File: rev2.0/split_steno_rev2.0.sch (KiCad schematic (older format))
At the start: 6 parts

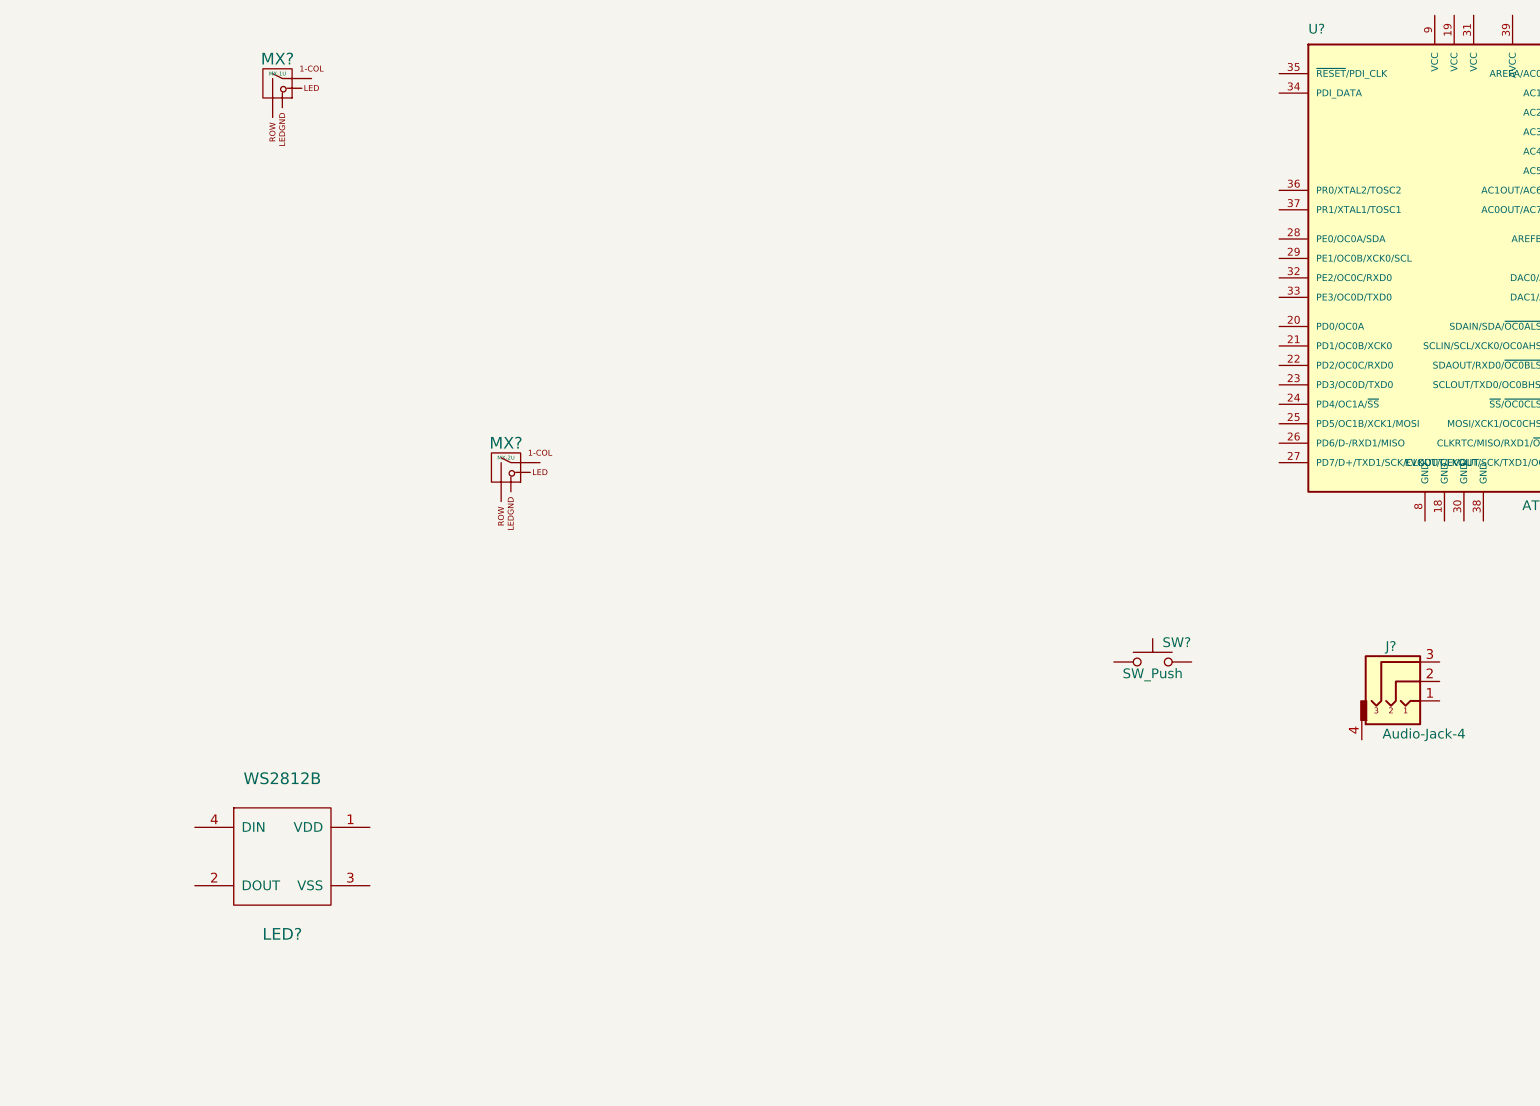
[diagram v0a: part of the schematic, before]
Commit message: switch and underglow matrix
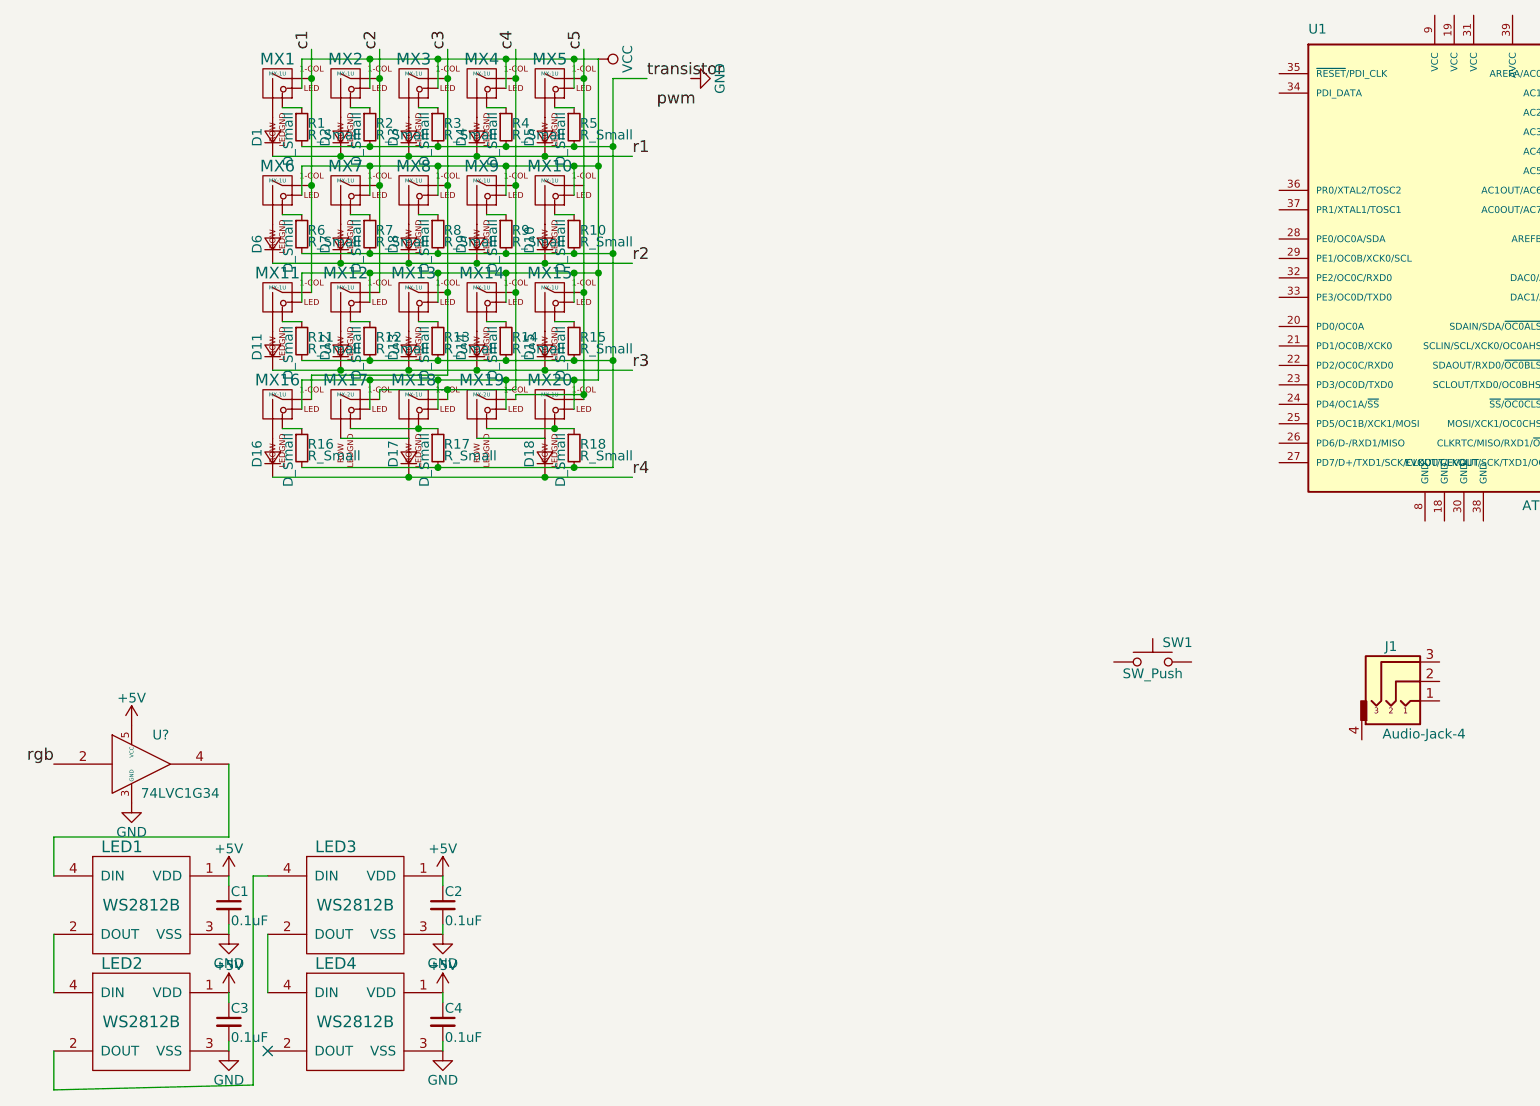
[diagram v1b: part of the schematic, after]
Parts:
- removed LED?: WS2812B, symbol WS2812B
- added C1, C2, C3, C4: 0.1uF, symbol C_Small
- added D1, D10, D11, D12, D13, D14, D15, D16, D17, D18, D2, D3, D4, D5, D6, D7, D8, D9: D_Small, symbol D_Small
- added LED1, LED2, LED3, LED4: WS2812B, symbol WS2812B
- added MX10, MX11, MX12, MX13, MX14, MX15, MX16, MX18, MX2, MX20, MX3, MX4, MX5, MX6, MX7, MX8, MX9: MX-1U, symbol MX-1U
- added MX19: MX-2U, symbol MX-2U
- added R1, R10, R11, R12, R13, R14, R15, R16, R17, R18, R2, R3, R4, R5, R6, R7, R8, R9: R_Small, symbol R_Small
- added U?: 74LVC1G34, symbol 74LVC1G34
- gave numbers to parts that had none: 5
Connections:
- net c1: now reaches MX1.1 (COL)
- net c1: now also MX11.1 (COL), MX6.1 (COL)
- net at MX1.2 (ROW): now also D1.2 (A)
- net VCC: now reaches MX1.3 (LED)
- net VCC: now also MX17.3 (LED), MX10.3 (LED), MX11.3 (LED), MX12.3 (LED), MX13.3 (LED), MX14.3 (LED), MX15.3 (LED), MX16.3 (LED), MX18.3 (LED), MX19.3 (LED), MX2.3 (LED), MX20.3 (LED), MX3.3 (LED), MX4.3 (LED), MX5.3 (LED), MX6.3 (LED), MX7.3 (LED), MX8.3 (LED), MX9.3 (LED)
- net at MX1.4 (LEDGND): now also R1.1
- net c4: now reaches MX17.1 (COL)
- net c4: now also MX14.1 (COL), MX18.1 (COL), MX4.1 (COL), MX9.1 (COL)
- net at MX17.2 (ROW): now also D17.2 (A), MX18.2 (ROW)
- net at MX17.4 (LEDGND): now also MX18.4 (LEDGND), R17.1
- new net: D2.2 (A), MX2.2 (ROW)
- new net: MX2.4 (LEDGND), R2.1
- new net: D3.2 (A), MX3.2 (ROW)
- new net: MX3.4 (LEDGND), R3.1
- new net: D4.2 (A), MX4.2 (ROW)
- new net: MX4.4 (LEDGND), R4.1
- new net: D5.2 (A), MX5.2 (ROW)
- new net: MX5.4 (LEDGND), R5.1
- new net: D18.2 (A), MX19.2 (ROW), MX20.2 (ROW)
- new net: MX19.4 (LEDGND), MX20.4 (LEDGND), R18.1
- new net: D6.2 (A), MX6.2 (ROW)
- new net: MX6.4 (LEDGND), R6.1
- new net: D7.2 (A), MX7.2 (ROW)
- new net: MX7.4 (LEDGND), R7.1
- new net: D8.2 (A), MX8.2 (ROW)
- new net: MX8.4 (LEDGND), R8.1
- new net: D9.2 (A), MX9.2 (ROW)
- new net: MX9.4 (LEDGND), R9.1
- new net: D10.2 (A), MX10.2 (ROW)
- new net: MX10.4 (LEDGND), R10.1
- new net: D11.2 (A), MX11.2 (ROW)
- new net: MX11.4 (LEDGND), R11.1
- new net: D12.2 (A), MX12.2 (ROW)
- new net: MX12.4 (LEDGND), R12.1
- new net: D13.2 (A), MX13.2 (ROW)
- new net: MX13.4 (LEDGND), R13.1
- new net: D14.2 (A), MX14.2 (ROW)
- new net: MX14.4 (LEDGND), R14.1
- new net: D15.2 (A), MX15.2 (ROW)
- new net: MX15.4 (LEDGND), R15.1
- new net: D16.2 (A), MX16.2 (ROW)
- new net: MX16.4 (LEDGND), R16.1
- new net: LED1.2 (DOUT), LED2.4 (DIN)
- new net: LED1.4 (DIN), U?.4
- new net: LED2.2 (DOUT), LED3.4 (DIN)
- new net: LED3.2 (DOUT), LED4.4 (DIN)
- new net +5V: C1.1, C2.1, C3.1, C4.1, LED1.1 (VDD), LED2.1 (VDD), LED3.1 (VDD), LED4.1 (VDD), U?.5 (VCC)
- new net GND: C1.2, C2.2, C3.2, C4.2, LED1.3 (VSS), LED2.3 (VSS), LED3.3 (VSS), LED4.3 (VSS), U?.3 (GND)
- new net c2: MX12.1 (COL), MX2.1 (COL), MX7.1 (COL)
- new net c3: MX13.1 (COL), MX16.1 (COL), MX3.1 (COL), MX8.1 (COL)
- new net c5: MX15.1 (COL), MX19.1 (COL), MX20.1 (COL), MX5.1 (COL)
- new net r1: D1.1 (K), D2.1 (K), D3.1 (K), D4.1 (K), D5.1 (K)
- new net r2: D10.1 (K), D6.1 (K), D7.1 (K), D8.1 (K), D9.1 (K)
- new net r3: D11.1 (K), D12.1 (K), D13.1 (K), D14.1 (K), D15.1 (K)
- new net r4: D16.1 (K), D17.1 (K), D18.1 (K)
- new net rgb: U?.2
- new net transistor: R1.2, R10.2, R11.2, R12.2, R13.2, R14.2, R15.2, R16.2, R17.2, R18.2, R2.2, R3.2, R4.2, R5.2, R6.2, R7.2, R8.2, R9.2
- no-connect marks 0 -> 1
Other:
- moved on the sheet: MX17

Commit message: some updates
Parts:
- removed C1, C2, C3, C4: 0.1uF, symbol C_Small
- added BT?: Battery, symbol Battery
- added BT?: Battery_Cell, symbol Battery_Cell
- added C? (x2): 4.7uF, symbol C
- added C? (x2): 1uF, symbol C
- added C? (x9): 0.1uF, symbol C
- added C?: 47uF, symbol C
- added D?: D_Schottky_x2_KCom_AAK, symbol D_Schottky_x2_KCom_AAK
- added F?: Fuse, symbol Fuse
- added J?: USB_C_Receptacle, symbol USB_C_Receptacle
- added JP? (x3): Jumper, symbol Jumper
- added P?: TC2030-IDC, symbol TC2030-IDC
- added R? (x2): 10k, symbol R
- added R? (x2): 470k, symbol R
- added R? (x4): R, symbol R
- added SW?: Switch-6P-2S2T, symbol Switch-6P-2S2T
- added U?: nRF24L01_module, symbol nRF24L01_module
- added U?: MCP73831, symbol MCP73831
- added U? (x2): MCP1700, TO_SOT_Packages_SMD:SOT-23, symbol MCP1700
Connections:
- net rgb is gone; now on net UNDER_LED: U?.2
- net +5V: now also C?.1, C?.1, C?.1, C?.1, C?.1, F?.2, R?.1, U?.3 (VI), U?.4 (VDD)
- net GND: now also SW1.1, U1.18 (GND), U1.30 (GND), U1.38 (GND), U1.8 (GND), BT?.2 (-), BT?.2 (-), C?.2, C?.2, C?.2, C?.2, C?.2, C?.2, C?.2, C?.2, C?.2, C?.2, C?.2, C?.2, C?.2, C?.2, J?.A1 (GND), J?.A12 (GND), J?.B1 (GND), J?.B12 (GND), P?.6 (P6), R?.2, R?.2, R?.2, R?.2, U?.1 (GND), U?.1 (GND), U?.2 (VSS), U?.2 (VSS)
- net VCC: now also U1.19 (VCC), U1.31 (VCC), U1.39 (AVCC), U1.9 (VCC), C?.1, C?.1, C?.1, C?.1, C?.1, C?.1, D?.3 (K), JP?.2, P?.2 (P2), R?.1, U?.1 (VDD)
- net UNDER_LED: now reaches U1.10 (SDAIN/SDA/~OC0ALS~/OC0A/PC0)
- net VBUS_CHECK: now reaches U1.11 (SCLIN/SCL/XCK0/OC0AHS/OC0B/PC1)
- net VBUS_CHECK: now also R?.1, R?.2
- net BAT_PROG: now reaches U1.12 (SDAOUT/RXD0/~OC0BLS~/OC0C/PC2)
- net BAT_PROG: now also R?.2
- net BAT_STAT: now reaches U1.13 (SCLOUT/TXD0/OC0BHS/OC0D/PC3)
- net BAT_STAT: now also U?.1 (STAT)
- net CSN: now reaches U1.14 (~SS~/~OC0CLS~/OC1A/PC4)
- net CSN: now also U?.4 (CSN)
- net MOSI: now reaches U1.15 (MOSI/XCK1/OC0CHS/OC1B/PC5)
- net MOSI: now also U?.6 (MOSI)
- net MISO: now reaches U1.16 (CLKRTC/MISO/RXD1/~OC0DLS~/PC6)
- net MISO: now also U?.7 (MISO)
- net SCK: now reaches U1.17 (EVOUT/CLKOUT/SCK/TXD1/OC0DHS/PC7)
- net SCK: now also U?.5 (SCK)
- net PDI: now reaches U1.34 (PDI_DATA)
- net PDI: now also P?.1 (P1)
- net RST: now reaches U1.35 (~RESET~/PDI_CLK)
- net RST: now also SW1.2, P?.5 (P5), R?.2
- net BAT_LVL: now reaches U1.5 (ADC9/PB1)
- net BAT_LVL: now also JP?.2, R?.1, R?.2
- net CE: now reaches U1.6 (DAC0/ADC10/PB2)
- net CE: now also U?.3 (CE)
- net IRQ: now reaches U1.7 (DAC1/ACD11/PB3)
- net IRQ: now also U?.8 (IRQ)
- net c1 renamed C1
- net c2 renamed C2
- net c3 renamed C3
- net c4 renamed C4
- net c5 renamed C5
- net r1 renamed R1
- net r2 renamed R2
- net r3 renamed R3
- net r4 renamed R4
- new net: R?.1, U?.5 (PROG)
- new net: F?.1, J?.A4 (VBUS), J?.A9 (VBUS), J?.B4 (VBUS), J?.B9 (VBUS)
- new net: J?.A5 (CC1), R?.1
- new net: J?.B3 (TX2-), J?.B5 (CC2), R?.1
- new net: C?.1, D?.1 (A), U?.2 (VO)
- new net +BATT: D?.2 (A), JP?.1, JP?.2, SW?.1, SW?.4
- new net BAT_IN: BT?.1 (+), C?.1, JP?.1, JP?.1, SW?.2, SW?.5, U?.2 (VO)
- new net BAT_LI_ION: BT?.1 (+), C?.1, R?.1, U?.3 (VBAT), U?.3 (VI)
- new net USB_L_D+: J?.A6 (D+), J?.B6 (D+)
- new net USB_L_D-: J?.A7 (D-), J?.B7 (D-)
- no-connect marks 1 -> 13
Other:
- moved on the sheet: D1, D10, D11, D12, D13, D14, D15, D16, D17, D18, D2, D3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

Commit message: switch to diodeless matrix, usb otg
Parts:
- removed D1, D10, D11, D12, D13, D14, D15, D16, D17, D18, D2, D3, D4, D5, D6, D7, D8, D9: D_Small, symbol D_Small
- removed J?: USB_C_Receptacle, symbol USB_C_Receptacle
- removed MX1, MX10, MX11, MX12, MX13, MX14, MX15, MX16, MX18, MX2, MX20, MX3, MX4, MX5, MX6, MX7, MX8, MX9: MX-1U, symbol MX-1U
- removed MX17, MX19: MX-2U, symbol MX-2U
- removed R1, R10, R11, R12, R13, R14, R15, R16, R17, R18, R2, R3, R4, R5, R6, R7, R8, R9: R_Small, symbol R_Small
- removed R?: R, symbol R
- added J?: USB_OTG, symbol USB_OTG
- added R? (x2): R, symbol R
- added SW? (x20): SW_Push, symbol SW_Push
- R? (x3): value R -> 100k
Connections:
- net GND: now also J1.4, J?.5 (GND), SW?.2, SW?.2, SW?.2, SW?.2, SW?.2, SW?.2, SW?.2, SW?.2, SW?.2, SW?.2, SW?.2, SW?.2, SW?.2, SW?.2, SW?.2, SW?.2, SW?.2, SW?.2, SW?.2, SW?.2
- net SDA: now reaches U1.28 (PE0/OC0A/SDA)
- net SDA: now also J1.3, R?.2
- net SCL: now reaches U1.29 (PE1/OC0B/XCK0/SCL)
- net SCL: now also J1.2, R?.2
- net +3V3: now reaches J1.1
- net +3V3: now also R?.1, R?.1
- net at F?.1: now also J?.1 (VBUS)
- net at R?.1: now also J?.4 (ID)
- new net KEY1: SW?.1
- new net KEY10: SW?.1
- new net KEY11: SW?.1
- new net KEY12: SW?.1
- new net KEY13: SW?.1
- new net KEY14: SW?.1
- new net KEY15: SW?.1
- new net KEY16: SW?.1
- new net KEY17: SW?.1, SW?.1
- new net KEY18: SW?.1, SW?.1
- new net KEY2: SW?.1
- new net KEY3: SW?.1
- new net KEY4: SW?.1
- new net KEY5: SW?.1
- new net KEY6: SW?.1
- new net KEY7: SW?.1
- new net KEY8: SW?.1
- new net KEY9: SW?.1
- new net USB_D+: J?.3 (D+)
- new net USB_D-: J?.2 (D-)
- no-connect marks 13 -> 6
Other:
- moved on the sheet: BT?, C?, D?, F?, J1, JP?, LED1, LED2, LED3, LED4, P?, R?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

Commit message: things
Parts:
- C14: renamed from C?; value 0.1uF -> 10uF
- R7, R9: renamed from R?; value R -> 4.7k
- gave numbers to parts that had none: 55
- renumbered SW1 to SW22, U1 to U5
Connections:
- net labels added: D+, D-
- net labels removed: USB_D+, USB_D-
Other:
- moved on the sheet: BT1, BT2, C1, C10, C11, C12, C13, C14, C2, C3, C4, C5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

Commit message: did footprint associations
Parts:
- BT1: footprint (none) -> Battery_Holders:Keystone_1058_1x2032-CoinCell
- BT2: footprint (none) -> Connectors_JST:JST_PH_S2B-PH-K_02x2.00mm_Angled
- C1, C10, C11, C12, C13, C14, C2, C3, C4, C5, C6, C7, C8, C9: footprint (none) -> Capacitors_SMD:C_0603_HandSoldering
- J1: footprint (none) -> Keebio-Parts:TRRS-PJ-320A
- LED1, LED2, LED3, LED4: footprint (none) -> WS2812B:WS2812B
- R1, R2, R3, R4, R5, R6, R7, R8, R9: footprint (none) -> Resistors_SMD:R_0603_HandSoldering
- SW1, SW10, SW11, SW12, SW13, SW14, SW15, SW16, SW17, SW18, SW2, SW3, SW4, SW5, SW6, SW7, SW8, SW9: footprint (none) -> Keebio-Parts:Hybrid_PCB_100H_Dual_hole
- SW19, SW20: footprint (none) -> Keebio-Parts:Hybrid_PCB_200H-dual-nosilk
- U5: footprint TQFP44 -> Housings_QFP:TQFP-44_10x10mm_Pitch0.8mm
- U6: footprint (none) -> nordic:NRF24L01-Module-SMD
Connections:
- no-connect marks 6 -> 7

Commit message: begin pcb file
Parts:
- D1: footprint (none) -> TO_SOT_Packages_SMD:SOT-23_Handsoldering
- F1: footprint (none) -> Fuse_Holders_and_Fuses:Fuse_SMD1206_HandSoldering
- J2: footprint (none) -> keyboard_parts:USB_miniB
- JP1, JP2, JP3: footprint (none) -> keyboard_parts:SOLDER_JUMPER_2
- P1: footprint (none) -> Connectors:Tag-Connect_TC2030-IDC-NL
- SW21: footprint (none) -> switch:SlideSwitch_C&K_JS202011CQN
- SW22: footprint (none) -> switch:SwitchPush_C&K_MultiFoot_RS-187R05A2-DS_And_PTS645_SMT
- U1: footprint (none) -> TO_SOT_Packages_SMD:SOT-353_SC-70-5_Handsoldering
- U2: footprint (none) -> TO_SOT_Packages_SMD:SOT-23-5_HandSoldering
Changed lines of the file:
@@
 F 0 "SW22" H 8475 5000 50  0000 L CNN
 F 1 "SW_Push" H 8425 4840 50  0000 C CNN
-F 2 "" H 8425 5100 50  0001 C CNN
+F 2 "switch:SwitchPush_C&K_MultiFoot_RS-187R05A2-DS_And_PTS645_SMT" H 8425 5100 50  0001 C CNN
 F 3 "" H 8425 5100 50  0001 C CNN
 	1    8425 4900
@@
 F 0 "U1" H 2375 5725 50  0000 C CNN
 F 1 "74LVC1G34" H 2475 5425 50  0000 C CNN
-F 2 "" H 2275 5575 50  0001 C CNN
+F 2 "TO_SOT_Packages_SMD:SOT-353_SC-70-5_Handsoldering" H 2275 5575 50  0001 C CNN
 F 3 "" H 2275 5575 50  0001 C CNN
 	1    2275 5575
@@
 F 0 "JP1" H 3225 1975 50  0000 C CNN
 F 1 "Jumper" H 3225 1745 50  0000 C CNN
-F 2 "" H 3225 1825 50  0001 C CNN
+F 2 "keyboard_parts:SOLDER_JUMPER_2" H 3225 1825 50  0001 C CNN
 F 3 "" H 3225 1825 50  0001 C CNN
 	1    3225 1825
@@
 F 0 "U2" H 2775 3500 60  0000 C CNN
 F 1 "MCP73831" H 3225 2800 60  0000 C CNN
-F 2 "" H 2975 3150 60  0001 C CNN
+F 2 "TO_SOT_Packages_SMD:SOT-23-5_HandSoldering" H 2975 3150 60  0001 C CNN
 F 3 "" H 2975 3150 60  0001 C CNN
 	1    2975 3150
@@
 F 0 "JP2" H 5425 2300 50  0000 C CNN
 F 1 "Jumper" H 5425 2070 50  0000 C CNN
-F 2 "" H 5425 2150 50  0001 C CNN
+F 2 "keyboard_parts:SOLDER_JUMPER_2" H 5425 2150 50  0001 C CNN
 F 3 "" H 5425 2150 50  0001 C CNN
 	1    5425 2150
@@
 F 0 "SW21" H 5350 1125 60  0000 C CNN
 F 1 "Switch-6P-2S2T" H 5300 1875 60  0000 C CNN
-F 2 "" H 5300 1675 60  0001 C CNN
+F 2 "switch:SlideSwitch_C&K_JS202011CQN" H 5300 1675 60  0001 C CNN
 F 3 "" H 5300 1675 60  0001 C CNN
 	1    5350 1475
@@
 F 0 "JP3" H 6900 1400 50  0000 C CNN
 F 1 "Jumper" H 6900 1170 50  0000 C CNN
-F 2 "" H 6900 1250 50  0001 C CNN
+F 2 "keyboard_parts:SOLDER_JUMPER_2" H 6900 1250 50  0001 C CNN
 F 3 "" H 6900 1250 50  0001 C CNN
 	1    6900 1250
@@
 F 0 "D1" H 7525 1775 50  0000 C CNN
 F 1 "D_Schottky_x2_KCom_AAK" H 7475 1975 50  0000 C CNN
-F 2 "" H 7475 1875 50  0001 C CNN
+F 2 "TO_SOT_Packages_SMD:SOT-23_Handsoldering" H 7475 1875 50  0001 C CNN
 F 3 "" H 7475 1875 50  0001 C CNN
 	1    7475 1875
@@
 F 0 "P1" H 6475 6325 40  0000 L CNN
 F 1 "TC2030-IDC" H 6525 6725 40  0000 C CNN
-F 2 "" H 6525 6525 60  0001 C CNN
+F 2 "Connectors:Tag-Connect_TC2030-IDC-NL" H 6525 6525 60  0001 C CNN
 F 3 "" H 6525 6525 60  0001 C CNN
 	1    6525 6525
@@
 F 0 "F1" V 14105 6700 50  0000 C CNN
 F 1 "Fuse" V 13950 6700 50  0000 C CNN
-F 2 "" V 13955 6700 50  0001 C CNN
+F 2 "Fuse_Holders_and_Fuses:Fuse_SMD1206_HandSoldering" V 13955 6700 50  0001 C CNN
 F 3 "" H 14025 6700 50  0001 C CNN
 	1    14025 6700
@@
 F 0 "J2" H 14275 7350 50  0000 L CNN
 F 1 "USB_OTG" H 14275 7250 50  0000 L CNN
-F 2 "" H 14625 6850 50  0001 C CNN
+F 2 "keyboard_parts:USB_miniB" H 14625 6850 50  0001 C CNN
 F 3 "" H 14625 6850 50  0001 C CNN
 	1    14475 6900
